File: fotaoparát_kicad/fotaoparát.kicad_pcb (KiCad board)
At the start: 4 copper layers, 13 parts, among them IC1 W25Q256JVEIQ, J1 Conn_01x15_Pin, J2 Micro_SD_Card_Det1, Q1 AO3400A

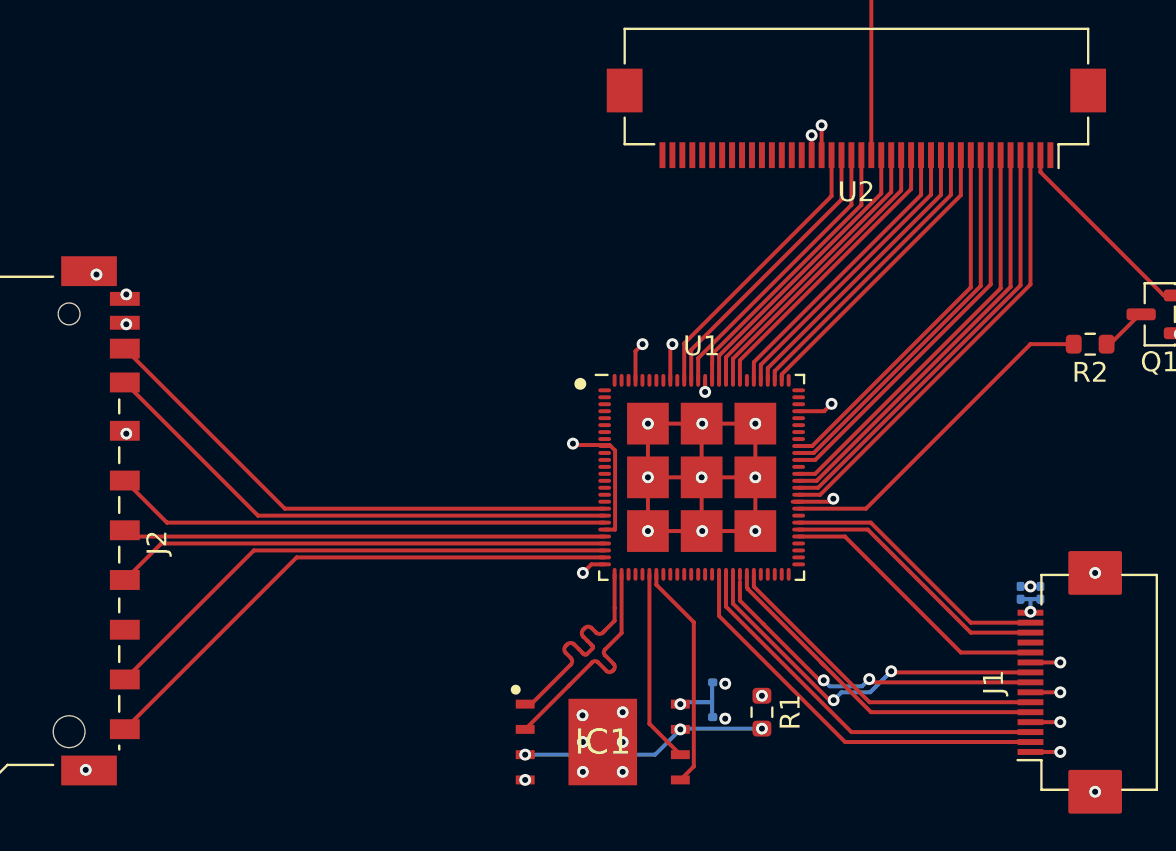
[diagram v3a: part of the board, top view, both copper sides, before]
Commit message: Upraveni routingu pro zlepseni kvality signalu
musim predelat cely konktor na display
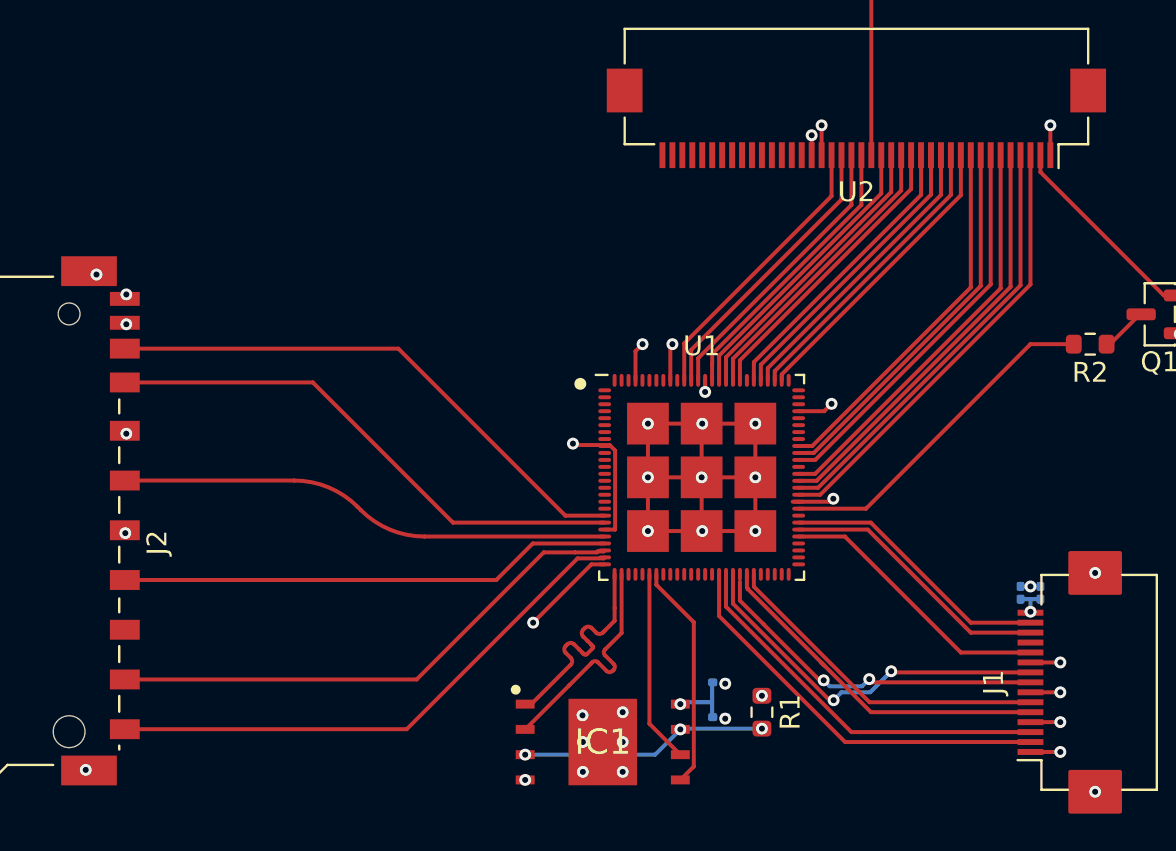
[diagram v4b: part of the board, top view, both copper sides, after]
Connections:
- net /cmd renamed /CMD
- net /dat2 renamed /DAT2
- net /dat3/cd renamed /DAT3/CD
- net /det renamed /DET
- J2 pad 4: /vdd -> +3.3V
- J2 pad 5: /clk -> /CLK
- J2 pad 7: /dat0 -> /DAT0
- J2 pad 8: /dat1 -> /DAT1
- U1 pad 18: /dat1 -> unconnected-(U1-GPIO17/ADC-Pad18)
- U1 pad 19: /dat0 -> /DAT1
- U1 pad 20: /clk -> /DAT0
- U1 pad 22: /vdd -> /CLK
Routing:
- net /DAT1: track 0.00 -> 27.6 mm
- net /dat1: track 27.5 -> 0.00 mm
- net /DAT0: track 0.00 -> 27.1 mm
- net /dat0: track 26.9 -> 0.00 mm
- net /clk: track 25.0 -> 0.00 mm
- net /CLK: track 0.00 -> 24.9 mm
- net /vdd: track 24.3 -> 0.00 mm
- net +3.3V: track 23.3 -> 28.5 mm, vias 12 -> 14
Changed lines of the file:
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@@
 	(net 94 "unconnected-(U1-GPIO1{slash}ADC-Pad1)")
 	(net 95 "unconnected-(U1-GPIO16{slash}ADC-Pad17)")
-	(net 96 "/vdd")
-	(net 97 "/dat0")
-	(net 98 "/dat2")
-	(net 99 "/det")
-	(net 100 "/dat1")
-	(net 101 "/dat3{slash}cd")
-	(net 102 "/cmd")
-	(net 103 "/clk")
+	(net 96 "/DAT0")
+	(net 97 "/DAT2")
+	(net 98 "/DET")
+	(net 99 "/DAT1")
+	(net 100 "/DAT3{slash}CD")
+	(net 101 "/CMD")
+	(net 102 "/CLK")
+	(net 103 "unconnected-(U1-GPIO17{slash}ADC-Pad18)")
 	(net 104 "Net-(U2-pin19)")
 	(footprint "Connector_Card:SD_TE_2041021"
@@
 			(size 1 1.5)
 			(layers "F.Cu" "F.Mask" "F.Paste")
-			(net 98 "/dat2")
+			(net 97 "/DAT2")
 			(pinfunction "DAT2")
 			(pintype "bidirectional")
@@
 			(size 1 1.5)
 			(layers "F.Cu" "F.Mask" "F.Paste")
-			(net 101 "/dat3{slash}cd")
+			(net 100 "/DAT3{slash}CD")
 			(pinfunction "DAT3/CD")
 			(pintype "bidirectional")
@@
 			(size 1 1.5)
 			(layers "F.Cu" "F.Mask" "F.Paste")
-			(net 102 "/cmd")
+			(net 101 "/CMD")
 			(pinfunction "CMD")
 			(pintype "input")
@@
 			(size 1 1.5)
 			(layers "F.Cu" "F.Mask" "F.Paste")
-			(net 96 "/vdd")
+			(net 7 "+3.3V")
 			(pinfunction "VDD")
 			(pintype "power_in")
@@
 			(size 1 1.5)
 			(layers "F.Cu" "F.Mask" "F.Paste")
-			(net 103 "/clk")
+			(net 102 "/CLK")
 			(pinfunction "CLK")
 			(pintype "input")
@@
 			(size 1 1.5)
 			(layers "F.Cu" "F.Mask" "F.Paste")
-			(net 97 "/dat0")
+			(net 96 "/DAT0")
 			(pinfunction "DAT0")
 			(pintype "bidirectional")
@@
 			(size 1 1.5)
 			(layers "F.Cu" "F.Mask" "F.Paste")
-			(net 100 "/dat1")
+			(net 99 "/DAT1")
 			(pinfunction "DAT1")
 			(pintype "bidirectional")
@@
 			(size 1 1.5)
 			(layers "F.Cu" "F.Mask" "F.Paste")
-			(net 99 "/det")
+			(net 98 "/DET")
 			(pinfunction "DET")
 			(pintype "passive")
@@
 			(size 0.2 0.65)
 			(layers "F.Cu" "F.Mask" "F.Paste")
-			(net 100 "/dat1")
+			(net 103 "unconnected-(U1-GPIO17{slash}ADC-Pad18)")
 			(pinfunction "GPIO17/ADC")
 			(pintype "bidirectional")
@@
 			(size 0.2 0.65)
 			(layers "F.Cu" "F.Mask" "F.Paste")
-			(net 97 "/dat0")
+			(net 99 "/DAT1")
 			(pinfunction "GPIO18/ADC")
 			(pintype "bidirectional")
@@
 			(size 0.2 0.65)
 			(layers "F.Cu" "F.Mask" "F.Paste")
-			(net 103 "/clk")
+			(net 96 "/DAT0")
 			(pinfunction "GPIO19/ADC")
 			(pintype "bidirectional")
@@
 			(size 0.2 0.65)
 			(layers "F.Cu" "F.Mask" "F.Paste")
-			(net 96 "/vdd")
+			(net 102 "/CLK")
 			(pinfunction "GPIO20/ADC")
 			(pintype "bidirectional")
@@
 			(size 0.2 0.65)
 			(layers "F.Cu" "F.Mask" "F.Paste")
-			(net 102 "/cmd")
+			(net 101 "/CMD")
 			(pinfunction "GPIO21/ADC")
 			(pintype "bidirectional")
@@
 			(size 0.2 0.65)
 			(layers "F.Cu" "F.Mask" "F.Paste")
-			(net 98 "/dat2")
+			(net 97 "/DAT2")
 			(pinfunction "GPIO22/ADC")
 			(pintype "bidirectional")
@@
 			(size 0.2 0.65)
 			(layers "F.Cu" "F.Mask" "F.Paste")
-			(net 99 "/det")
+			(net 98 "/DET")
 			(pinfunction "GPIO23/ADC")
 			(pintype "bidirectional")
@@
 	)
 	(segment
+		(start 127.475 86.475)
+		(end 127.5 86.5)
+		(width 0.2)
+		(layer "F.Cu")
+		(net 7)
+	)
+	(segment
 		(start 163.088427 84.77)
 		(end 163.07 84.77)
@@
 	)
 	(segment
-		(start 151.595 88.07)
+		(start 148 91)
 		(end 150.93 88.07)
 		(width 0.2)
@@
 	)
 	(segment
-		(start 150.93 88.07)
-		(end 150.5 88.5)
+		(start 127.475 86.355)
+		(end 127.475 86.475)
 		(width 0.2)
 		(layer "F.Cu")
@@
 	)
 	(segment
+		(start 174 67.5)
+		(end 174 66)
+		(width 0.2)
+		(layer "F.Cu")
+		(net 7)
+	)
+	(segment
 		(start 151.595 86.32)
 		(end 152.12 86.32)
@@
 		(net 7)
 	)
+	(segment
+		(start 150.93 88.07)
+		(end 151.595 88.07)
+		(width 0.2)
+		(layer "F.Cu")
+		(net 7)
+	)
 	(via
 		(at 165 56.5)
@@
 	)
 	(via
+		(at 127.5 86.5)
+		(size 0.6)
+		(drill 0.3)
+		(layers "F.Cu" "B.Cu")
+		(net 7)
+	)
+	(via
 		(at 159.5 94.675)
 		(size 0.6)
@@
 	)
 	(via
-		(at 150.5 88.5)
+		(at 148 91)
+		(size 0.6)
+		(drill 0.3)
+		(layers "F.Cu" "B.Cu")
+		(net 7)
+	)
+	(via
+		(at 174 66)
 		(size 0.6)
 		(drill 0.3)
@@
 	)
 	(segment
-		(start 127.475 86.355)
-		(end 127.79 86.67)
+		(start 136.925 78.925)
+		(end 143.97 85.97)
 		(width 0.2)
 		(layer "F.Cu")
@@
 	)
 	(segment
-		(start 127.79 86.67)
-		(end 151.595 86.67)
+		(start 143.97 85.97)
+		(end 151.595 85.97)
 		(width 0.2)
 		(layer "F.Cu")
@@
 	(segment
 		(start 127.475 78.925)
-		(end 134.17 85.62)
+		(end 127.55 79)
+		(width 0.2)
+		(layer "F.Cu")
+		(net 96)
+	)
+	(segment
+		(start 127.475 78.925)
+		(end 136.925 78.925)
+		(width 0.2)
+		(layer "F.Cu")
+		(net 96)
+	)
+	(segment
+		(start 150.106322 87.468)
+		(end 151.196322 87.468)
 		(width 0.2)
 		(layer "F.Cu")
@@
 	)
 	(segment
-		(start 134.17 85.62)
-		(end 151.595 85.62)
+		(start 127.475 93.855)
+		(end 142.145 93.855)
 		(width 0.2)
 		(layer "F.Cu")
@@
 	)
 	(segment
-		(start 133.96 87.37)
+		(start 151.546 87.419)
 		(end 151.595 87.37)
 		(width 0.2)
 		(layer "F.Cu")
+		(net 97)
+	)
+	(segment
+		(start 148.532 87.468)
+		(end 150.106322 87.468)
+		(width 0.2)
+		(layer "F.Cu")
+		(net 97)
+	)
+	(segment
+		(start 151.245322 87.419)
+		(end 151.546 87.419)
+		(width 0.2)
+		(layer "F.Cu")
+		(net 97)
+	)
+	(segment
+		(start 151.196322 87.468)
+		(end 151.245322 87.419)
+		(width 0.2)
+		(layer "F.Cu")
+		(net 97)
+	)
+	(segment
+		(start 142.145 93.855)
+		(end 148.532 87.468)
+		(width 0.2)
+		(layer "F.Cu")
+		(net 97)
+	)
+	(segment
+		(start 141.645 96.355)
+		(end 127.475 96.355)
+		(width 0.2)
+		(layer "F.Cu")
 		(net 98)
 	)
 	(segment
-		(start 127.475 93.855)
-		(end 133.96 87.37)
+		(start 151.546 87.769)
+		(end 150.231 87.769)
 		(width 0.2)
 		(layer "F.Cu")
@@
 	)
 	(segment
-		(start 127.475 96.355)
-		(end 136.11 87.72)
+		(start 150.231 87.769)
+		(end 141.645 96.355)
 		(width 0.2)
 		(layer "F.Cu")
-		(net 99)
+		(net 98)
 	)
 	(segment
-		(start 136.11 87.72)
-		(end 151.595 87.72)
+		(start 151.595 87.72)
+		(end 151.546 87.769)
+		(width 0.2)
+		(layer "F.Cu")
+		(net 98)
+	)
+	(segment
+		(start 127.475 77.225)
+		(end 141.225 77.225)
 		(width 0.2)
 		(layer "F.Cu")
@@
 	)
 	(segment
-		(start 135.52 85.27)
-		(end 151.595 85.27)
+		(start 141.225 77.225)
+		(end 149.62 85.62)
 		(width 0.2)
 		(layer "F.Cu")
-		(net 100)
+		(net 99)
 	)
 	(segment
-		(start 127.475 77.225)
-		(end 135.52 85.27)
+		(start 149.62 85.62)
+		(end 151.595 85.62)
 		(width 0.2)
 		(layer "F.Cu")
-		(net 100)
+		(net 99)
 	)
 	(segment
 		(start 127.475 88.855)
-		(end 129.31 87.02)
+		(end 146.145 88.855)
 		(width 0.2)
 		(layer "F.Cu")
-		(net 102)
+		(net 101)
 	)
 	(segment
-		(start 129.31 87.02)
+		(start 147.98 87.02)
 		(end 151.595 87.02)
 		(width 0.2)
 		(layer "F.Cu")
+		(net 101)
+	)
+	(segment
+		(start 146.145 88.855)
+		(end 147.98 87.02)
+		(width 0.2)
+		(layer "F.Cu")
+		(net 101)
+	)
+	(segment
+		(start 135.991039 83.855)
+		(end 127.475 83.855)
+		(width 0.2)
+		(layer "F.Cu")
 		(net 102)
 	)
 	(segment
-		(start 127.475 83.855)
-		(end 129.59 85.97)
+		(start 151.595 86.67)
+		(end 142.533961 86.67)
 		(width 0.2)
 		(layer "F.Cu")
-		(net 103)
+		(net 102)
 	)
 	(segment
-		(start 129.59 85.97)
-		(end 151.595 85.97)
+		(start 139.35198 85.35198)
+		(end 139.173019 85.173019)
+		(width 0.2)
+		(layer "F.Cu")
+		(net 102)
+	)
+	(arc
+		(start 139.35198 85.35198)
+		(mid 140.811885 86.327458)
+		(end 142.533961 86.67)
 		(width 0.2)
 		(layer "F.Cu")
-		(net 103)
+		(net 102)
+	)
+	(arc
+		(start 139.173019 85.173019)
+		(mid 137.713114 84.197542)
+		(end 135.991039 83.855)
+		(width 0.2)
+		(layer "F.Cu")
+		(net 102)
 	)
 	(segment

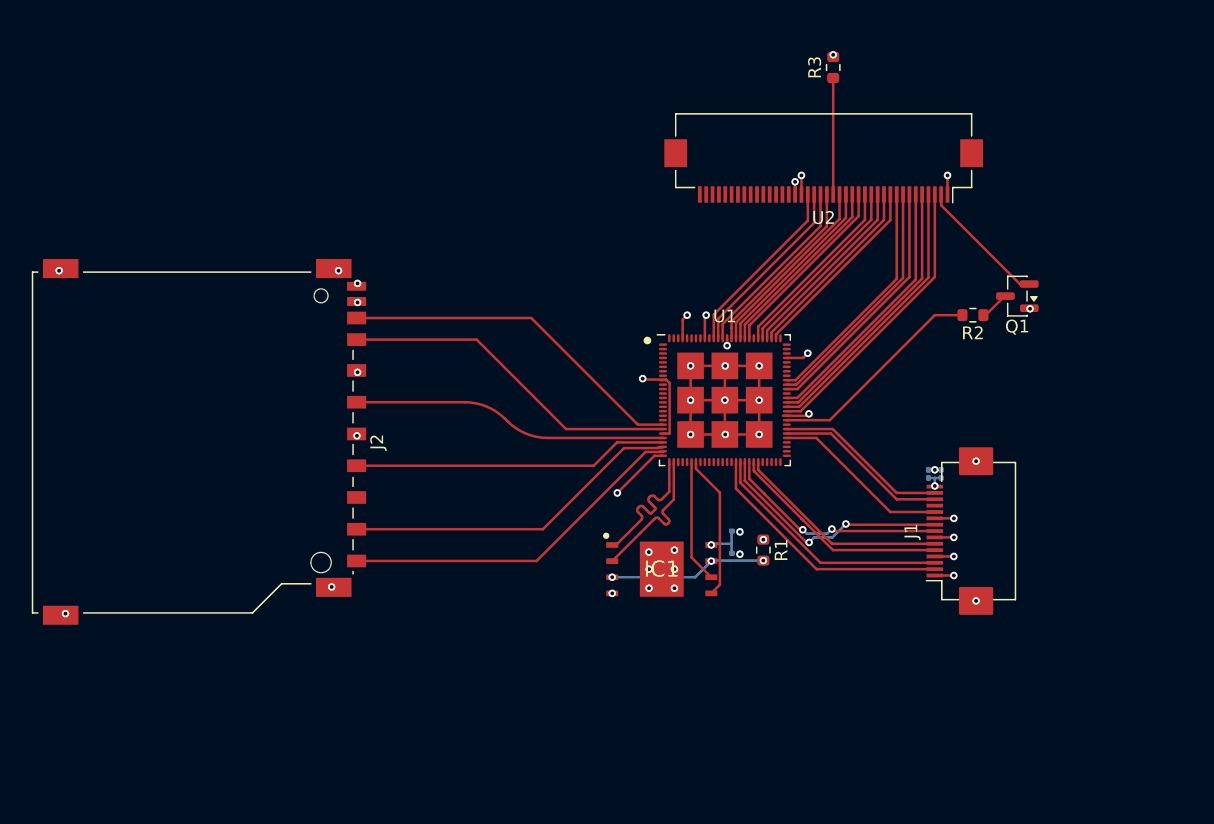
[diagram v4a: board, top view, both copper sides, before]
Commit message: Tech zmen je tolik ze ani nevim co napsat Rerouting v podstate vseho, znovu predelani displaye, flash, sd kartoveho holderu
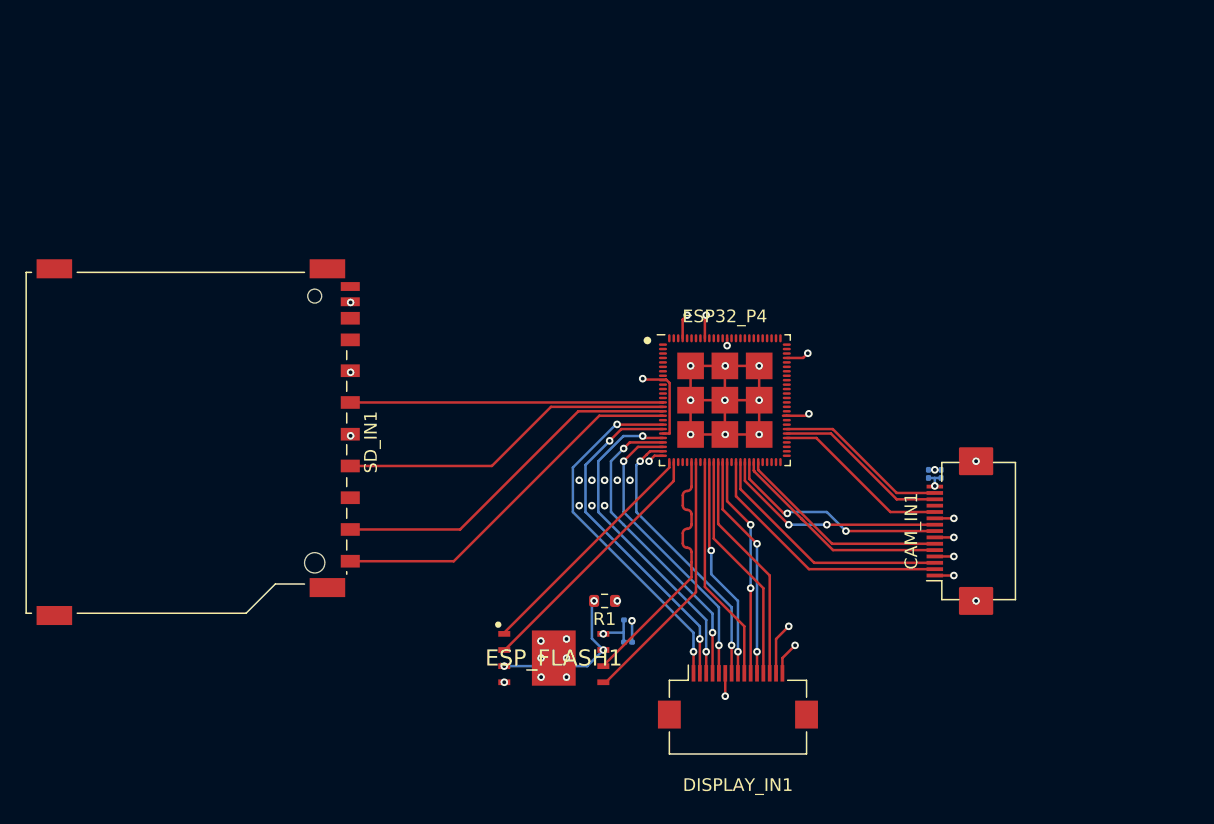
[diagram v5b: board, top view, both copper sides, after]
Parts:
- removed Q1: AO3400A, Package_TO_SOT_SMD:SOT-23
- removed R2: 100R, Resistor_SMD:R_0603_1608Metric
- removed R3: 10k, Resistor_SMD:R_0603_1608Metric
- removed U2: ~, Connector_FFC-FPC:Hirose_FH12-40S-0.5SH_1x40-1MP_P0.50mm_Horizontal
- added DISPLAY_IN1: Conn_01x15_Socket, Connector_FFC-FPC:Hirose_FH12-15S-0.5SH_1x15-1MP_P0.50mm_Horizontal, F.Cu at (157.5, 107.0)
- moved R1 13.1 mm to (147.0, 99.5), turned to 180 degrees
- moved C1 11.0 mm to (148.8, 102.8)
- moved C2 11.0 mm to (148.8, 101.0)
- moved ESP_FLASH1 11.0 mm to (143.0, 104.0)
- moved SD_IN1 0.50 mm to (115.0, 87.0)
- renumbered J1 to CAM_IN1, U1 to ESP32_P4, IC1 to ESP_FLASH1, J2 to SD_IN1
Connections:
- net Net-(IC1-CLK) renamed /FLASH_CLK
- net Net-(IC1-DI_(IO0)) renamed /FLASH_DI_(IO0)
- net Net-(IC1-DO_(IO1)_1) renamed /FLASH_(IO1)_1
- net Net-(IC1-DO_(IO1)_2) renamed /FLASH_DO_(IO1)_2
- net Net-(IC1-/CS) renamed /FLASH_/CS
- ESP32_P4 pad 11: unconnected-(U1-GPIO10/ADC-Pad11) -> /DAT1
- ESP32_P4 pad 12: unconnected-(U1-GPIO11/ADC-Pad12) -> /DAT0
- ESP32_P4 pad 14: unconnected-(U1-GPIO13/ADC-Pad14) -> /CLK
- ESP32_P4 pad 15: unconnected-(U1-GPIO14/ADC-Pad15) -> /CMD
- ESP32_P4 pad 16: unconnected-(U1-GPIO15/ADC-Pad16) -> /DAT2
- ESP32_P4 pad 17: unconnected-(U1-GPIO16/ADC-Pad17) -> /DET
- ESP32_P4 pad 19: /DAT1 -> /DEBUG
- ESP32_P4 pad 20: /DAT0 -> /RST
- ESP32_P4 pad 22: /CLK -> /I2C_SDA
- ESP32_P4 pad 23: /CMD -> /INT
- ESP32_P4 pad 24: /DAT2 -> /I2C_SCL
- ESP32_P4 pad 25: /DET -> /LED_PWM
- ESP32_P4 pad 35: unconnected-(U1-DSI_DATAP1-Pad35) -> /DSI_DATAP1
- ESP32_P4 pad 36: unconnected-(U1-DSI_DATAN1-Pad36) -> /DSI_DATAN1
- ESP32_P4 pad 37: unconnected-(U1-DSI_CLKN-Pad37) -> /DSI_CLKN
- ESP32_P4 pad 38: unconnected-(U1-DSI_CLKP-Pad38) -> /DSI_CLKP
- ESP32_P4 pad 39: unconnected-(U1-DSI_DATAP0-Pad39) -> /DSI_DATAP0
- ESP32_P4 pad 40: unconnected-(U1-DSI_DATAN0-Pad40) -> /DSI_DATAN0
- ESP32_P4 pad 61: Net-(U1-GPIO31) -> unconnected-(ESP32_P4-GPIO31-Pad61)
- ESP32_P4 pad 63: /D15 -> unconnected-(ESP32_P4-GPIO32-Pad63)
- ESP32_P4 pad 64: /D14 -> unconnected-(ESP32_P4-GPIO33-Pad64)
- ESP32_P4 pad 65: /D13 -> unconnected-(ESP32_P4-GPIO34-Pad65)
- ESP32_P4 pad 66: /D12 -> unconnected-(ESP32_P4-GPIO35-Pad66)
- ESP32_P4 pad 68: /D11 -> unconnected-(ESP32_P4-GPIO36-Pad68)
- ESP32_P4 pad 69: /D10 -> unconnected-(ESP32_P4-GPIO37-Pad69)
- ESP32_P4 pad 70: /D9 -> unconnected-(ESP32_P4-GPIO38-Pad70)
- ESP32_P4 pad 80: /D8 -> unconnected-(ESP32_P4-GPIO39-Pad80)
- ESP32_P4 pad 81: /D7 -> unconnected-(ESP32_P4-GPIO40-Pad81)
- ESP32_P4 pad 82: /D6 -> unconnected-(ESP32_P4-GPIO41-Pad82)
- ESP32_P4 pad 83: /D5 -> unconnected-(ESP32_P4-GPIO42-Pad83)
- ESP32_P4 pad 84: /D4 -> unconnected-(ESP32_P4-GPIO43-Pad84)
- ESP32_P4 pad 86: /D3 -> unconnected-(ESP32_P4-GPIO44-Pad86)
- ESP32_P4 pad 87: /D2 -> unconnected-(ESP32_P4-GPIO45-Pad87)
- ESP32_P4 pad 88: /D1 -> unconnected-(ESP32_P4-GPIO46-Pad88)
- ESP32_P4 pad 89: /D0 -> unconnected-(ESP32_P4-GPIO47-Pad89)
- ESP32_P4 pad 90: /WR -> unconnected-(ESP32_P4-GPIO48-Pad90)
- ESP32_P4 pad 92: /RS/DC -> unconnected-(ESP32_P4-GPIO49/ADC-Pad92)
- ESP32_P4 pad 93: /CS -> unconnected-(ESP32_P4-GPIO50/ADC-Pad93)
- ESP32_P4 pad 94: /RESET -> unconnected-(ESP32_P4-GPIO51/ADC-Pad94)
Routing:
- net /DEBUG: track 0.00 -> 28.6 mm, vias 0 -> 2
- net /DAT1: track 27.6 -> 0.00 mm
- net /RST: track 0.00 -> 27.4 mm, vias 0 -> 2
- net /DAT0: track 27.1 -> 0.00 mm
- net /I2C_SDA: track 0.00 -> 26.2 mm, vias 0 -> 2
- net /INT: track 0.00 -> 24.7 mm, vias 0 -> 2
- net /I2C_SCL: track 0.00 -> 23.4 mm, vias 0 -> 2
- net /D15: track 22.5 -> 0.00 mm
- net /LED_PWM: track 0.00 -> 22.1 mm, vias 0 -> 2
- net /D14: track 21.9 -> 0.00 mm
- net /D13: track 21.3 -> 0.00 mm
- net /D12: track 20.7 -> 0.00 mm
- net /D11: track 19.8 -> 0.00 mm
- net /D10: track 19.2 -> 0.00 mm
- net /D9: track 18.6 -> 0.00 mm
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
